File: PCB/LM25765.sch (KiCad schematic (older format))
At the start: 10 parts

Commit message: Started thinking through power supply
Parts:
- removed C?: 22uF, Capacitors:1206, symbol Device:C_Small
- removed C?: 1uF, Capacitors:0603, symbol Device:C_Small
- U?: value LM2576S-3.3 -> LM2576S-12
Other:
- moved on the sheet: C?

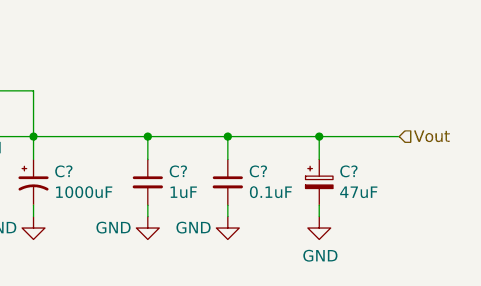
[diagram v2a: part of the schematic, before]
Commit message: Added battery voltage sense
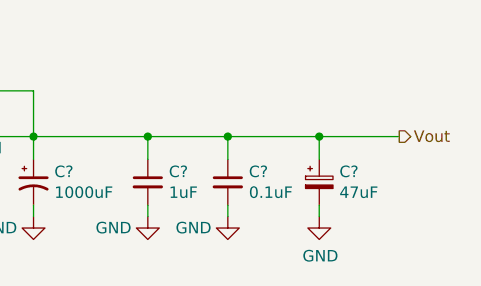
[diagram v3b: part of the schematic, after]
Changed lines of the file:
@@
 Text HLabel 4300 3650 0    50   Input ~ 0
 Vin
-Text HLabel 7900 3850 2    50   Input ~ 0
+Text HLabel 7900 3850 2    50   Output ~ 0
 Vout
 $Comp
